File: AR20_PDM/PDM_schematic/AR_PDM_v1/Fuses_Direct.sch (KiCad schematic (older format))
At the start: 13 parts, among them U31 INA233

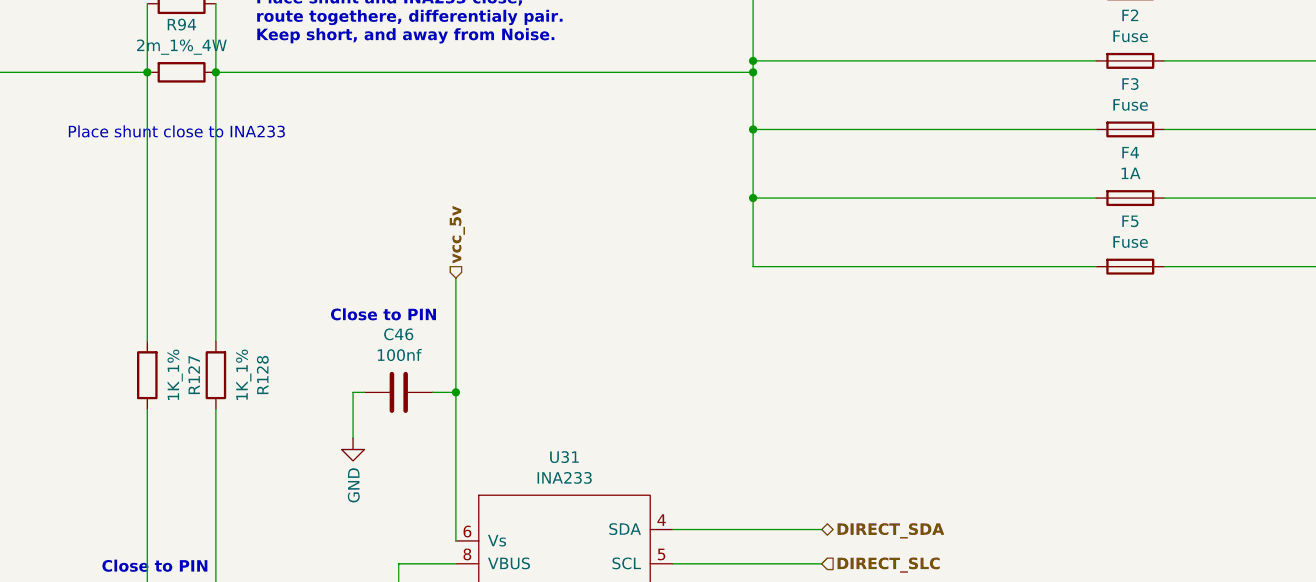
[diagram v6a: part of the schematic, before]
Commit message: shematics adjustments, and fixing values and names
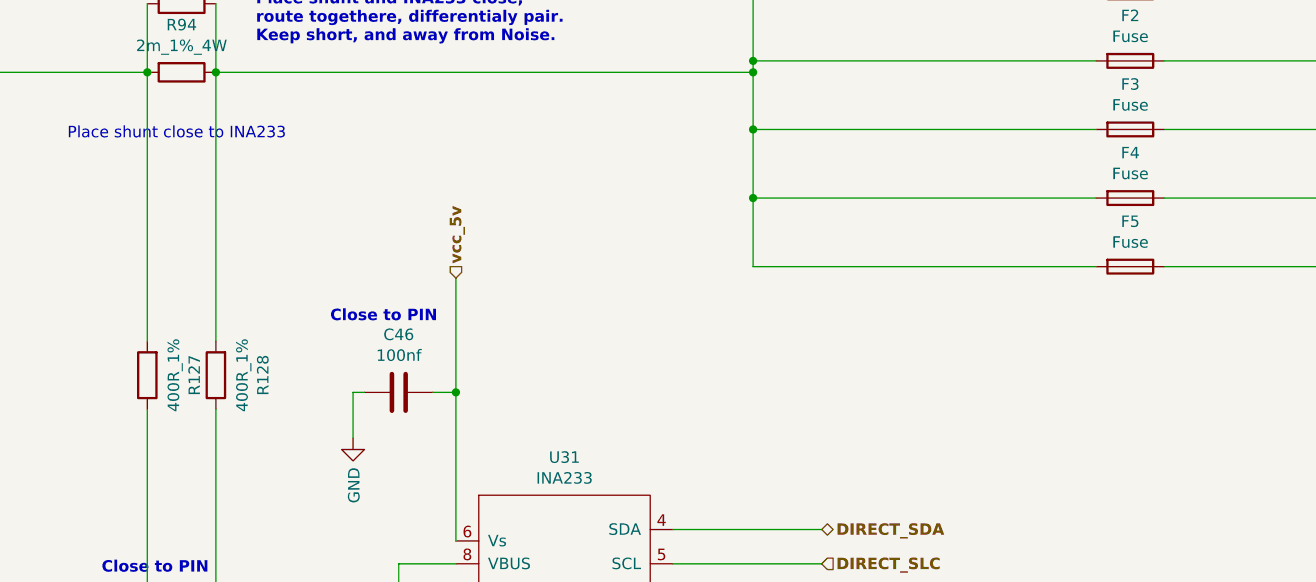
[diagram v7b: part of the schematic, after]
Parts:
- F4: value 1A -> Fuse
- R127, R128: value 1K_1% -> 400R_1%
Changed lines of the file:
@@
 P 7600 3550
 F 0 "F4" V 7403 3550 50  0000 C CNN
-F 1 "1A" V 7494 3550 50  0000 C CNN
+F 1 "Fuse" V 7494 3550 50  0000 C CNN
 F 2 "AR_PDM_v1:FuseHolder" V 7530 3550 50  0001 C CNN
 F 3 "~" H 7600 3550 50  0001 C CNN
@@
 AR Path="/5DE4D361/5EED49CD" Ref="R127"  Part="1"
 F 0 "R127" V 3093 4325 50  0000 C CNN
-F 1 "1K_1%" V 3184 4325 50  0000 C CNN
+F 1 "400R_1%" V 3184 4325 50  0000 C CNN
 F 2 "Resistor_SMD:R_0603_1608Metric" V 3230 4325 50  0001 C CNN
 F 3 "~" H 3300 4325 50  0001 C CNN
@@
 AR Path="/5DE4D361/5EED49C7" Ref="R128"  Part="1"
 F 0 "R128" V 3393 4325 50  0000 C CNN
-F 1 "1K_1%" V 3484 4325 50  0000 C CNN
+F 1 "400R_1%" V 3484 4325 50  0000 C CNN
 F 2 "Resistor_SMD:R_0603_1608Metric" V 3530 4325 50  0001 C CNN
 F 3 "~" H 3600 4325 50  0001 C CNN
